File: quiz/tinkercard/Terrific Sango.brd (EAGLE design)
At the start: 159.6 x 118.5 mm, 19 parts, among them U1 ARDUINO-UNO-R3-SHIELD

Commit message: feat: complete basic quiz wred hardware schematics and code
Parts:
- added R10: 1k, Tinkercad:RESAD1016W63L850D250B
- added R9: 100, Tinkercad:RESAD1016W63L850D250B
- R1, R2, R3, R4: value 1k -> 100
- moved D2 6.45 mm to (130.5, 105.8)
- moved D3 6.45 mm to (140.3, 104.9)
- moved R5 6.45 mm to (153.2, 92.8)
- moved R1 6.45 mm to (19.7, 25.3)
- moved R3 6.45 mm to (20.1, 16.7)
- moved U1 6.45 mm to (47.9, 60.2)
- moved D1 6.45 mm to (109.7, 109.2)
- moved D4 6.45 mm to (151.8, 105.0)
- moved S1 6.45 mm to (29.0, 109.5)
- moved S2 6.45 mm to (53.4, 109.6)
- moved S5 6.45 mm to (73.0, 114.7)
- moved R6 6.45 mm to (152.9, 76.8)
- moved S3 6.45 mm to (63.1, 109.7)
- moved S4 6.45 mm to (42.4, 109.7)
- moved R2 6.45 mm to (20.3, 21.6)
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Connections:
- new net S5_P: R10.2, S5.2
- net U1_5V: now also S6.2; no longer S6.3
- net U1_GND: now also R9.2
- net U1_RX: now also R9.1, S6.3, S6.4; no longer S6.1
- net U1_TX: now also R10.1; no longer S5.2
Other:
- board size 159.6 x 118.5 mm -> 159.6 x 121.7 mm

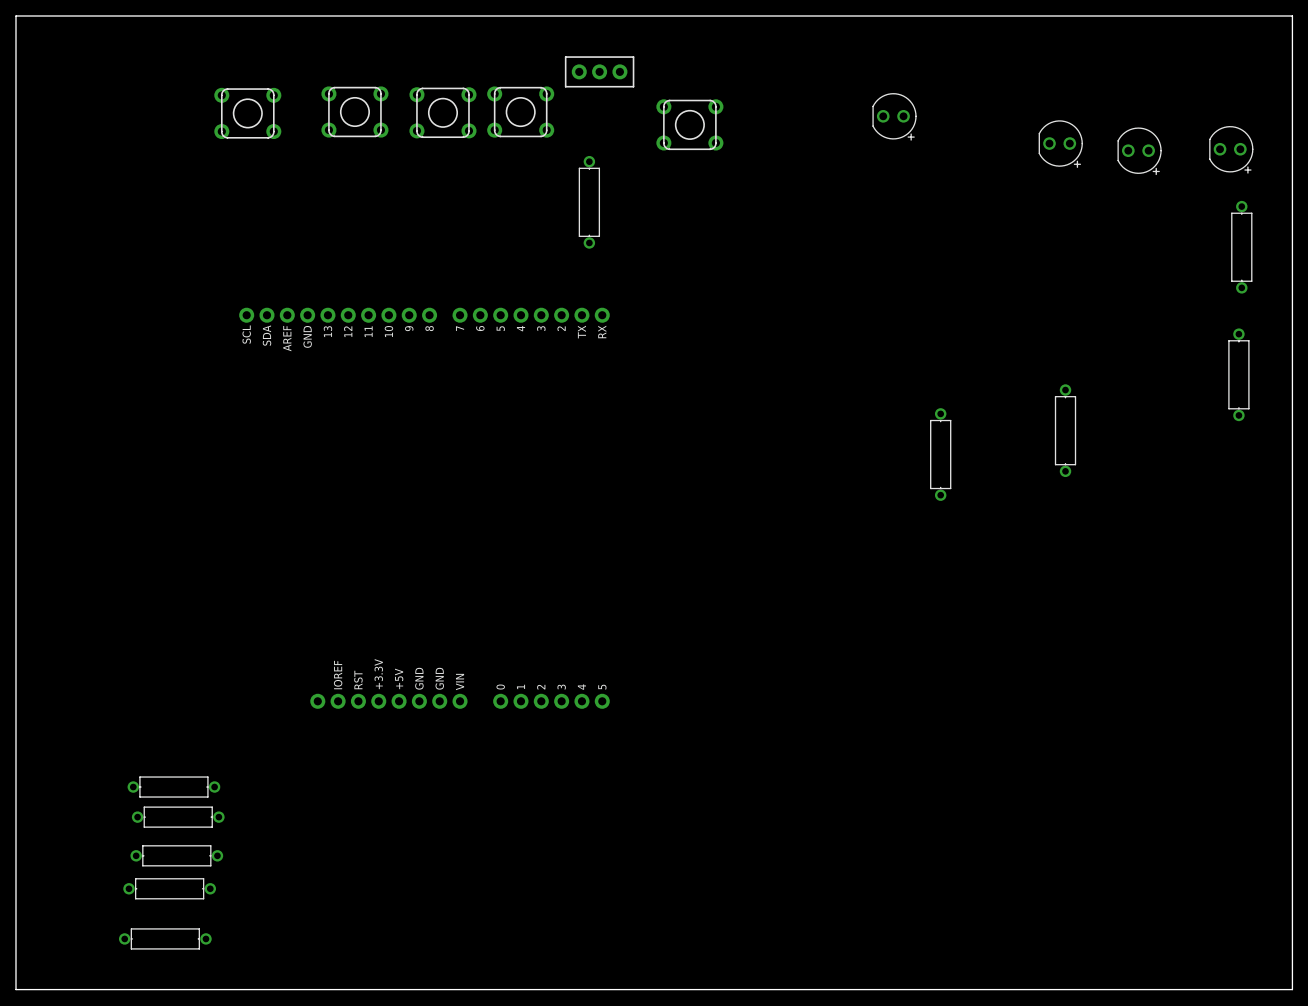
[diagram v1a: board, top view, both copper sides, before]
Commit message: feat: add circuit diagram png and pretify the circuit
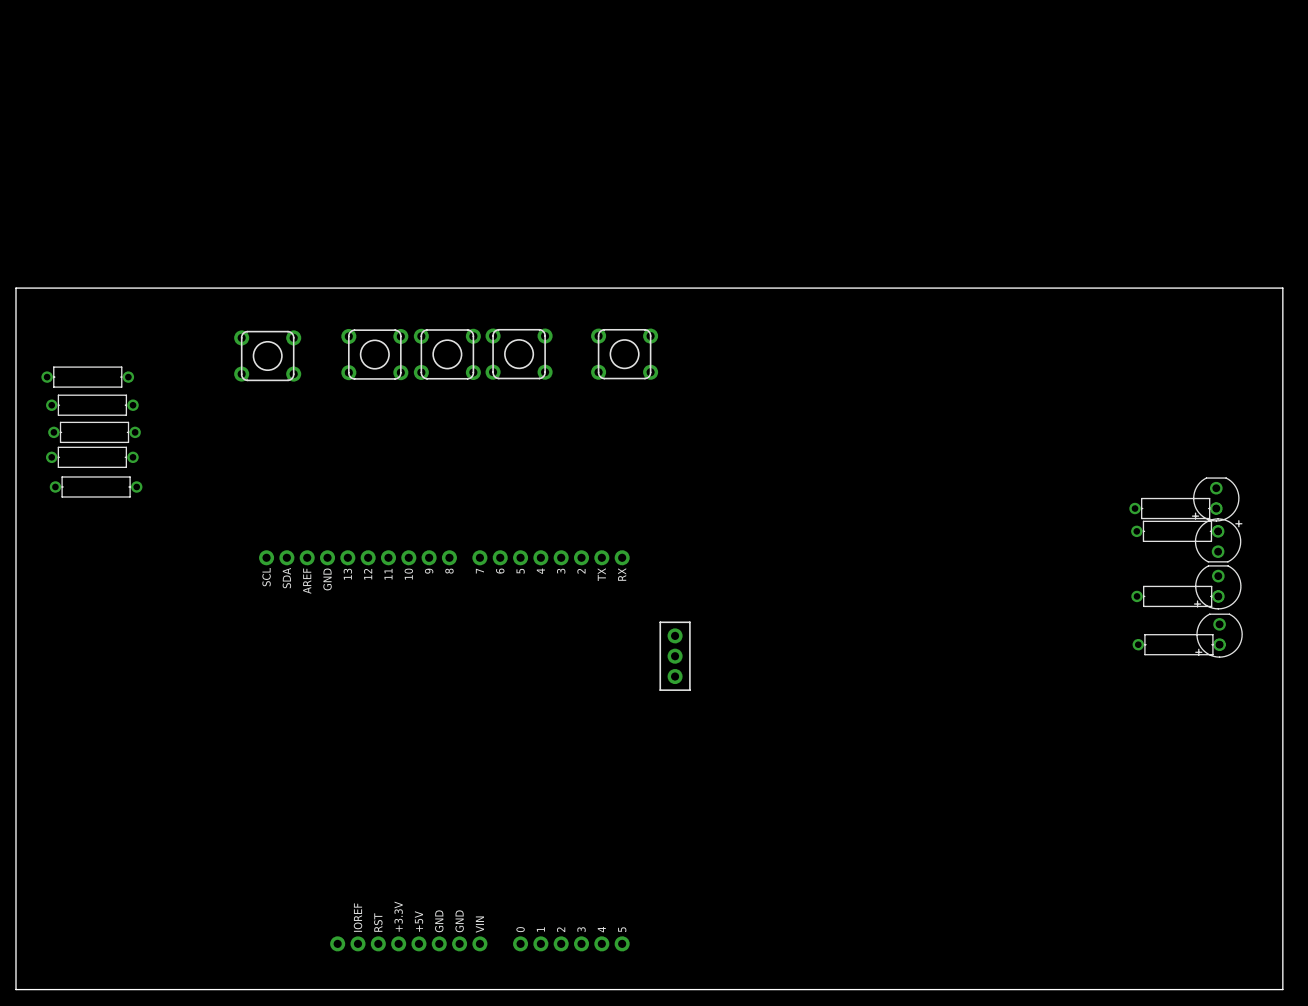
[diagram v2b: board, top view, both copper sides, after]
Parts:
- removed R9: 100, Tinkercad:RESAD1016W63L850D250B
- R10: value 1k -> 100
- moved S5 73.6 mm to (82.4, 41.7), turned to 270 degrees
- moved R10 66.4 mm to (8.97, 76.6), turned to 360 degrees
- moved D1 62.5 mm to (150.0, 61.4), turned to 90 degrees
- moved D3 61.3 mm to (150.4, 44.4), turned to 90 degrees
- moved R4 61.2 mm to (9.55, 73.0), turned to 180 degrees
- moved D4 54.6 mm to (150.3, 50.4), turned to 90 degrees
- moved D2 53.5 mm to (150.3, 56.0), turned to -90 degrees
- moved R3 47.2 mm to (10.0, 62.8), turned to 180 degrees
- moved R2 46.2 mm to (9.55, 66.5), turned to 180 degrees
- moved R1 45.4 mm to (9.81, 69.6), turned to 180 degrees
- moved R5 44.4 mm to (145.2, 49.1), turned to 0 degrees
- moved R6 34.6 mm to (145.4, 43.1), turned to 0 degrees
- moved S1 30.4 mm to (31.5, 79.2)
- moved S4 30.4 mm to (44.9, 79.4)
- moved U1 30.4 mm to (50.4, 29.8)
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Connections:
- net U1_5V: now also S6.1
- net U1_D10: now also R2.1; no longer R4.1
- net U1_D12: now also R4.1; no longer R2.1
- net U1_D13: now also R10.2; no longer R1.1
- net U1_D4: now also R6.1; no longer R5.1
- net U1_D5: now also R5.1; no longer R6.1
- net U1_GND: now also R10.1; no longer R9.2
- net U1_RX: now also R1.1; no longer R9.1
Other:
- board size 159.6 x 121.7 mm -> 158.4 x 87.7 mm
